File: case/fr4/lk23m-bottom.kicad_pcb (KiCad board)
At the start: 2 copper layers, 76.2 x 119.1 mm, 8 parts

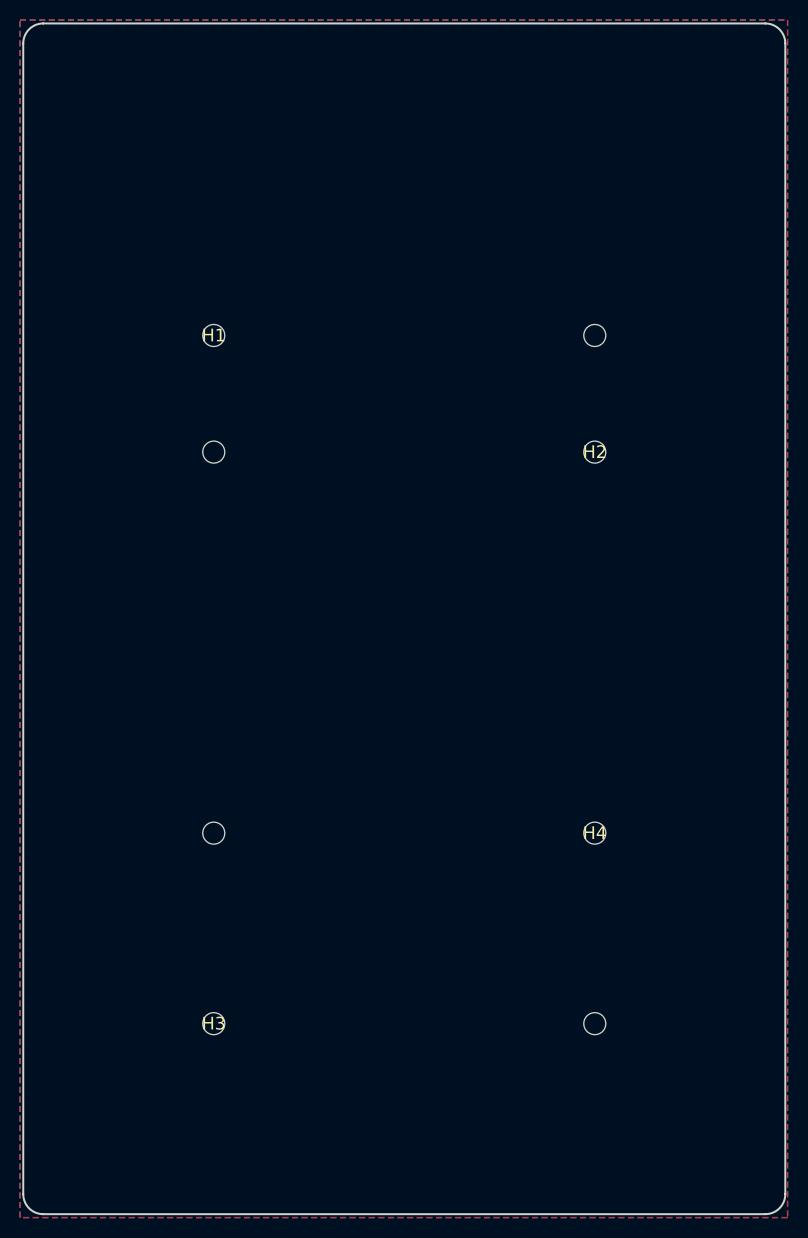
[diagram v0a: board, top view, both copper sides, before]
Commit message: Model should be done, we should just look at exporting keyboard.pretty as a library
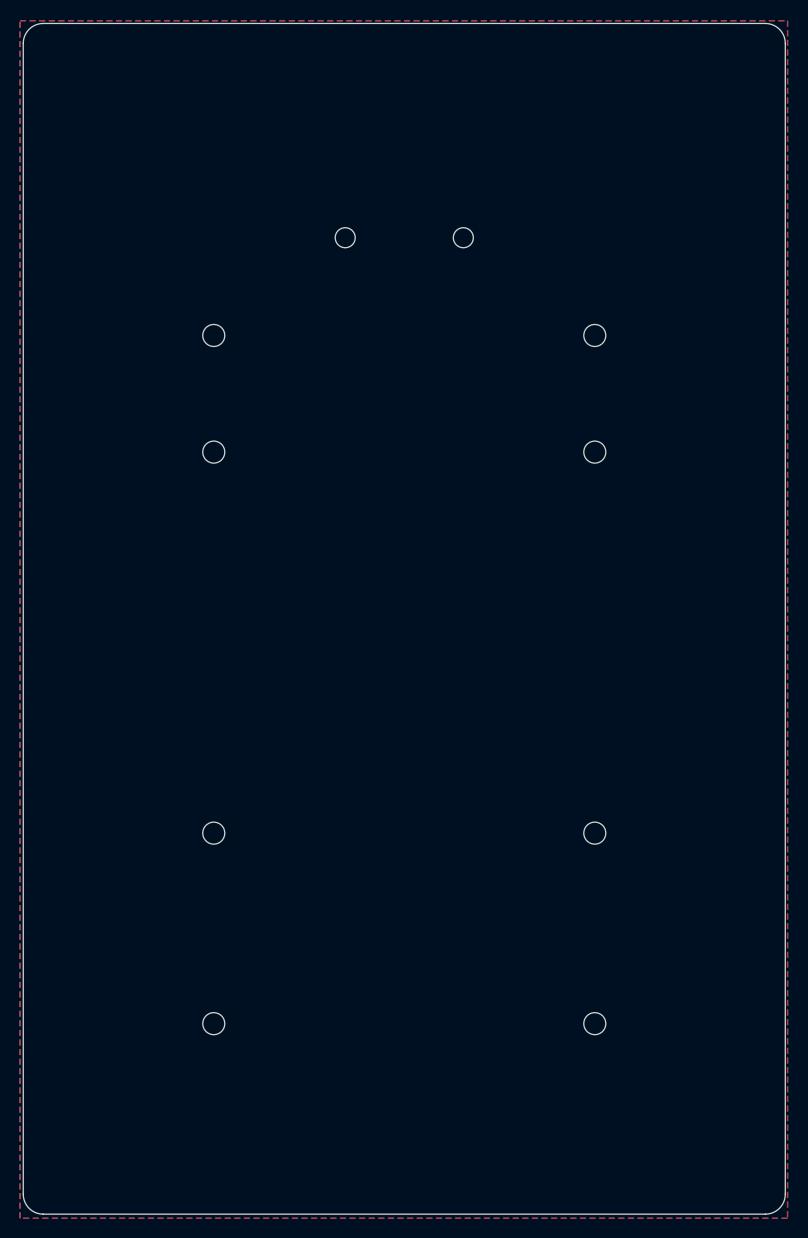
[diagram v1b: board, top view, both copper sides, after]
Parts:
- added H10: MountingHole_2mm, MountingHole:MountingHole_2mm, B.Cu at (72.6, 50.0)
- added H9: MountingHole_2mm, MountingHole:MountingHole_2mm, F.Cu at (60.8, 50.0)
- H1, H2, H3, H4, H5, H6, H7, H8: value (none) -> MountingHole_2.2mm_M2_ISO14580; footprint (none) -> MountingHole:MountingHole_2.2mm_M2_ISO14580
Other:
- board text added: "LK23M"
- board text added: "LambdaKB.dev"
